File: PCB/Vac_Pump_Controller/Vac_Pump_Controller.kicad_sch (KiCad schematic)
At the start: 21 parts, among them J1 Conn_01x04_Socket, J1A Conn_01x04_Pin, J2 Conn_01x02_Socket, J2A Conn_01x02_Pin, J3 Conn_01x08_Socket, J3A Conn_01x08_Pin, J4 AC Plug, J5 DIN-6, J6 Conn_01x06_Socket, J6A Conn_01x06_Pin, J7 DIN-6, K1 Dual Relay Module, SW1 RotaryEncoder_Switch_MP, SW2 Pwr Switch, U1 WeMos D1 Mini32, U2 JXI 1.28in Round LCD

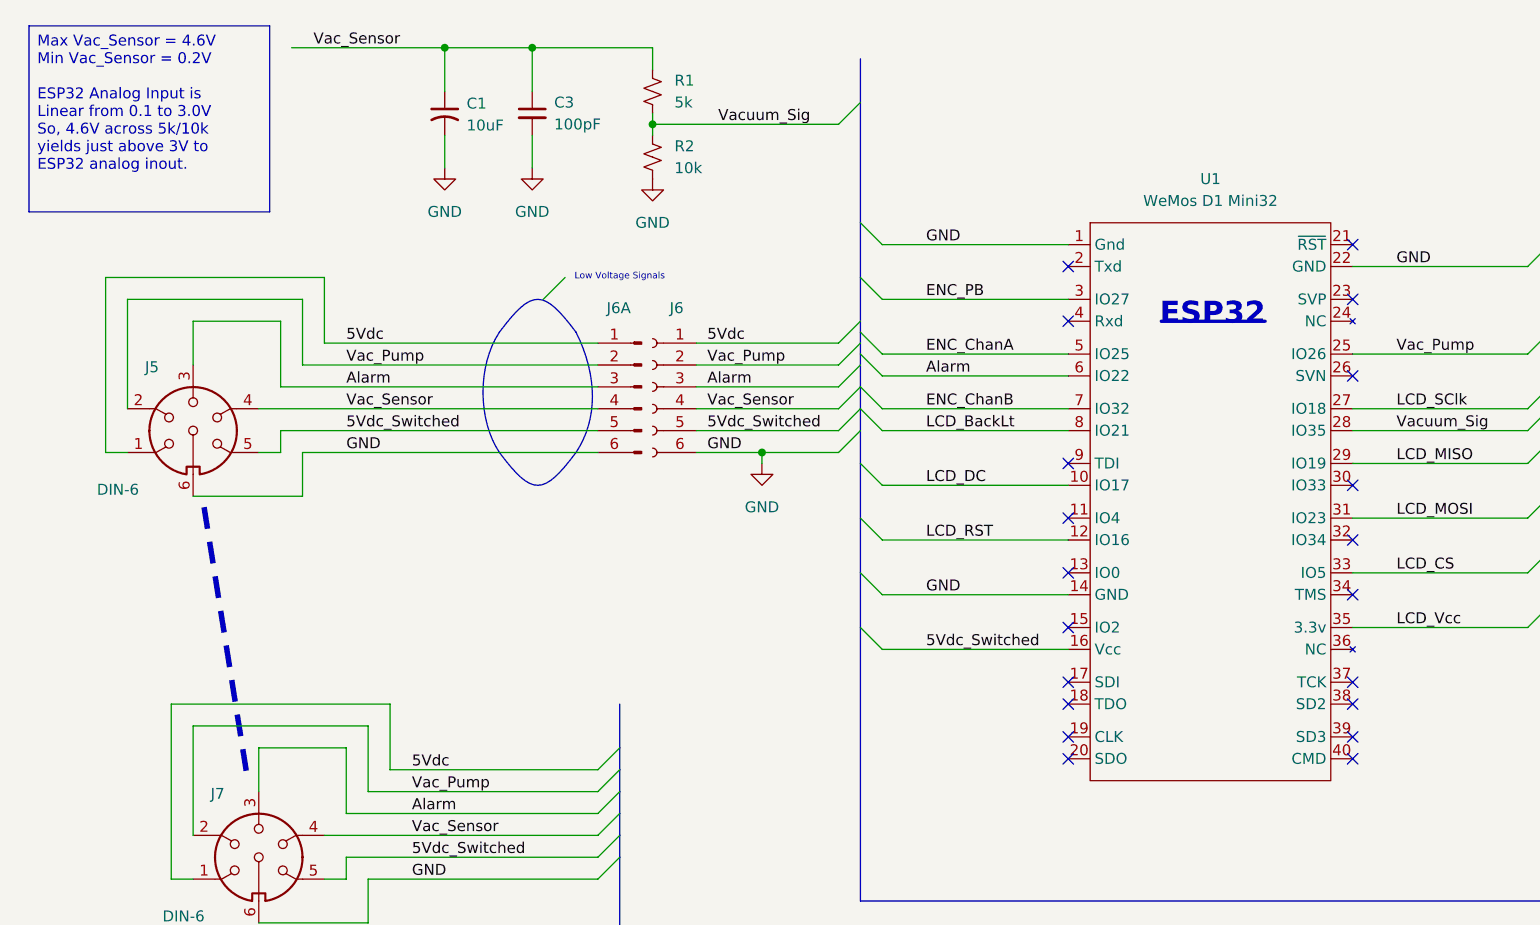
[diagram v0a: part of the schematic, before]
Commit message: PCB: swap ESP32 WeMos symbol for P-NUCLEO-WB55 (ST Morpho) in schematic
In-place symbol clone keeps identical pin geometry so every existing wire,
net-label and no-connect stays attached. Pin names -> WB55 functions, pin
numbers -> ST Morpho refs (CN7/CN10). Validated: kicad-cli sch erc reports
40 violations, identical to the pre-swap baseline (zero new). MCU power stays
on 5Vdc_Switched; MISO kept but marked n/c (write-only panel).

Co-Authored-By: Claude Opus 4.8 (1M context) <noreply@anthropic.com>
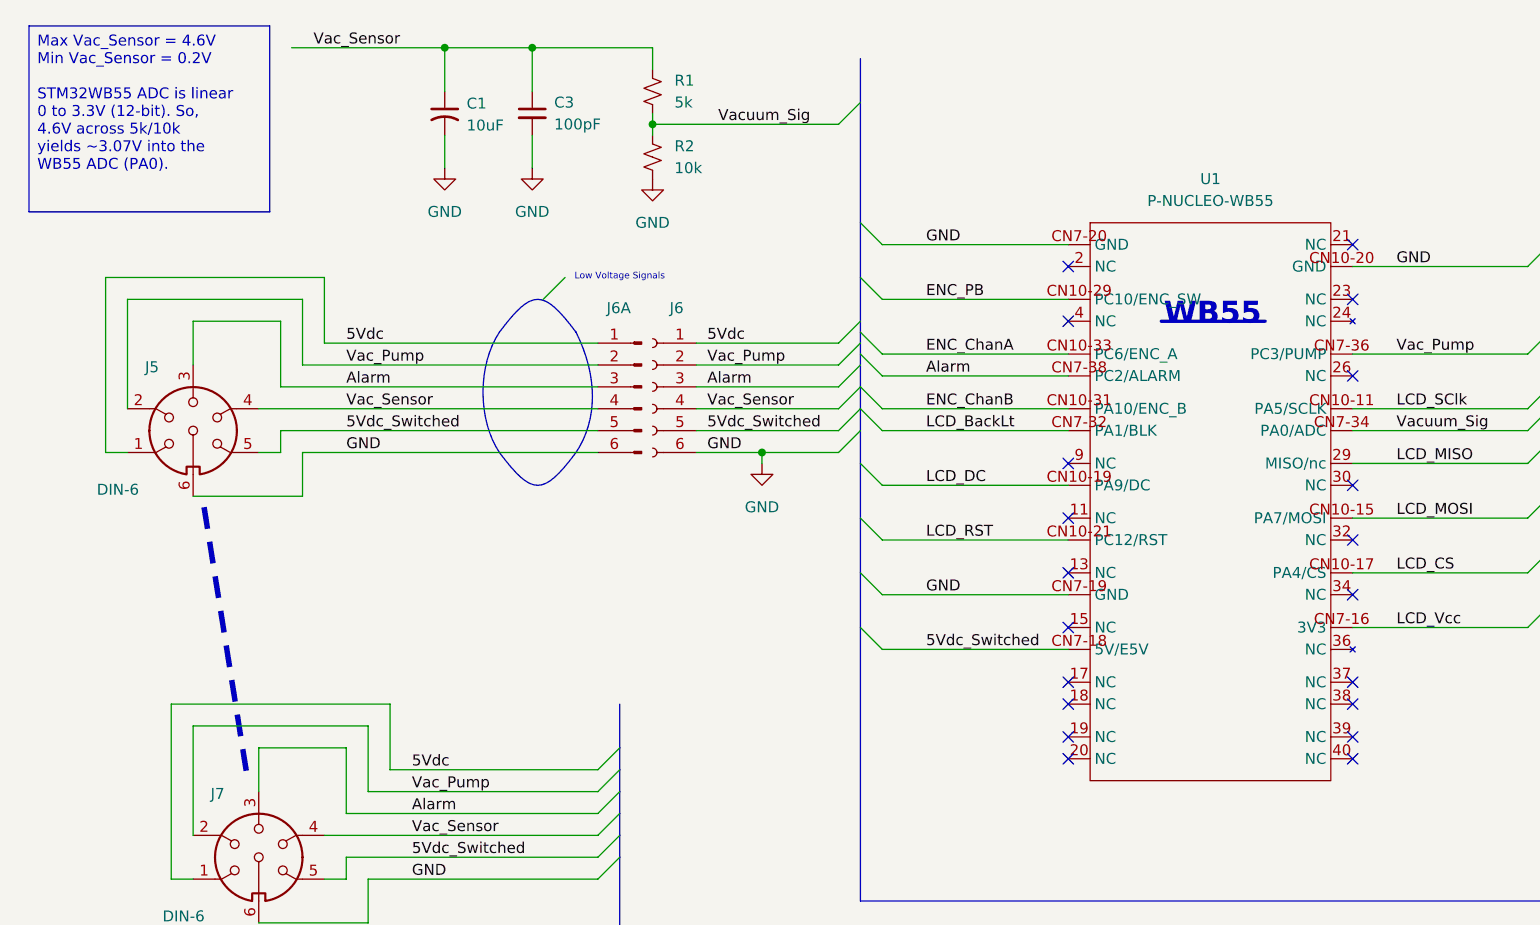
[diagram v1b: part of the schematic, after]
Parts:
- U1: value WeMos D1 Mini32 -> P-NUCLEO-WB55; symbol JK_And_Sons:WeMos_D1_Mini32 -> JK_And_Sons:P_NUCLEO_WB55
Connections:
- net 5Vdc_Switched: now also U1.CN7-18 (5V/E5V); no longer U1.16 (Vcc)
- net Alarm: now also U1.CN7-38 (PC2/ALARM); no longer U1.6 (IO22)
- net ENC_ChanA: now also U1.CN10-33 (PC6/ENC_A); no longer U1.5 (IO25)
- net ENC_ChanB: now also U1.CN10-31 (PA10/ENC_B); no longer U1.7 (IO32)
- net ENC_PB: now also U1.CN10-29 (PC10/ENC_SW); no longer U1.3 (IO27)
- net GND: now also U1.CN10-20 (GND), U1.CN7-19 (GND), U1.CN7-20 (GND); no longer U1.1 (Gnd), U1.14 (GND), U1.22 (GND)
- net LCD_BackLt: now also U1.CN7-32 (PA1/BLK); no longer U1.8 (IO21)
- net LCD_CS: now also U1.CN10-17 (PA4/CS); no longer U1.33 (IO5)
- net LCD_DC: now also U1.CN10-19 (PA9/DC); no longer U1.10 (IO17)
- net LCD_MOSI: now also U1.CN10-15 (PA7/MOSI); no longer U1.31 (IO23)
- net LCD_RST: now also U1.CN10-21 (PC12/RST); no longer U1.12 (IO16)
- net LCD_SClk: now also U1.CN10-11 (PA5/SCLK); no longer U1.27 (IO18)
- net LCD_Vcc: now also U1.CN7-16 (3V3); no longer U1.35 (3.3v)
- net Vac_Pump: now also U1.CN7-36 (PC3/PUMP); no longer U1.25 (IO26)
- net Vacuum_Sig: now also U1.CN7-34 (PA0/ADC); no longer U1.28 (IO35)
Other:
- note added: "WB55"
- note removed: "ESP32"
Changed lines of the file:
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@@
 		)
 	)
-	(text "ESP32"
+	(text "WB55"
 		(exclude_from_sim no)
 		(at 153.924 50.038 0)
@@
 		)
 	)
-	(text_box "Max Vac_Sensor = 4.6V\nMin Vac_Sensor = 0.2V\n\nESP32 Analog Input is\nLinear from 0.1 to 3.0V\nSo, 4.6V across 5k/10k\nyields just above 3V to\nESP32 analog inout."
+	(text_box "Max Vac_Sensor = 4.6V\nMin Vac_Sensor = 0.2V\n\nSTM32WB55 ADC is linear\n0 to 3.3V (12-bit). So,\n4.6V across 5k/10k\nyields ~3.07V into the\nWB55 ADC (PA0)."
 		(exclude_from_sim no)
 		(at 16.51 16.51 0)
@@
 	)
 	(symbol
-		(lib_id "JK_And_Sons:WeMos_D1_Mini32")
+		(lib_id "JK_And_Sons:P_NUCLEO_WB55")
 		(at 139.7 39.37 0)
 		(unit 1)
@@
 			)
 		)
-		(property "Value" "WeMos D1 Mini32"
+		(property "Value" "P-NUCLEO-WB55"
 			(at 153.67 36.83 0)
 			(effects
@@
 		(pin "21"
 		)
-		(pin "22"
+		(pin "CN10-20"
 		)
 		(pin "23"
@@
 		(pin "24"
 		)
-		(pin "25"
+		(pin "CN7-36"
 		)
 		(pin "26"
 		)
-		(pin "27"
+		(pin "CN10-11"
 		)
-		(pin "28"
+		(pin "CN7-34"
 		)
 		(pin "29"
@@
 		(pin "30"
 		)
-		(pin "31"
+		(pin "CN10-15"
 		)
 		(pin "32"
 		)
-		(pin "33"
+		(pin "CN10-17"
 		)
 		(pin "18"
@@
 		(pin "34"
 		)
-		(pin "35"
+		(pin "CN7-16"
 		)
 		(pin "19"
@@
 		(pin "20"
 		)
-		(pin "16"
+		(pin "CN7-18"
 		)
 		(pin "17"
@@
 		(pin "11"
 		)
-		(pin "3"
+		(pin "CN10-29"
 		)
-		(pin "14"
+		(pin "CN7-19"
 		)
 		(pin "2"
@@
 		(pin "13"
 		)
-		(pin "5"
+		(pin "CN10-33"
 		)
 		(pin "9"
 		)
-		(pin "12"
+		(pin "CN10-21"
 		)
-		(pin "6"
+		(pin "CN7-38"
 		)
-		(pin "1"
+		(pin "CN7-20"
 		)
 		(pin "36"
@@
 		(pin "4"
 		)
-		(pin "7"
+		(pin "CN10-31"
 		)
-		(pin "10"
+		(pin "CN10-19"
 		)
-		(pin "8"
+		(pin "CN7-32"
 		)
 		(instances

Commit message: PCB: tidy WB55 symbol label placement
Move the U1 net-labels outward along their existing wire stubs (right column
+12.7mm, left column -3.8mm) so they clear the longer WB55 pin numbers, and
remove the redundant 'WB55' watermark that overlapped two pin names. Only label
positions changed (wires/pins untouched) -> ERC unchanged at 40 (baseline) and
netlist connectivity verified identical (16 nets on U1, Morpho pin refs intact).

Co-Authored-By: Claude Opus 4.8 (1M context) <noreply@anthropic.com>
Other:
- note removed: "WB55"

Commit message: EVT1: calibrate vacuum readout + sensor front-end decoupling
Firmware (stm32/zephyrwb):
- Compile out CONFIG_VAC_SIM: read the real MPXV4115V on PA0/ADC1_IN5.
- Two-point calibration of the readout against the VB2200 manifold gauge with
  the fitted 3.94k/6.8k divider: atmosphere = 0 inHg @ 4044 counts, full vacuum
  = 29 inHg @ 709 counts (divider ratio and VREF cancel in the fit).
- Fix the gauge needle to track the calibrated value on the correct face angle
  (0 inHg at dial start, 30 under vacuum), aligned with the setpoint bugs.
- Enable CONFIG_LV_COLOR_16_SWAP to fix the GC9A01 RGB565 byte-swap color cast.

PCB (Vac_Pump_Controller):
- New Sensor_End hierarchical sheet: 3-pin MPXV4115V header with 10uF + 10nF
  supply decoupling and a 4-conductor cable connector back to the WB55.
- Add C4 10nF from the ADC divider tap to GND at the MCU (S&H / anti-alias).

.gitignore: exclude editor local-history and KiCad reports/lock files.

Co-Authored-By: Claude Opus 4.8 <noreply@anthropic.com>
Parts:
- added C4: 10nF, symbol Device:C_Small_US
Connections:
- net GND: now also C4.2
- net Vacuum_Sig: now also C4.1
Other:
- added sheet Sensor_End (Sensor_End.kicad_sch)
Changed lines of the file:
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@@
+		)
+	)
+	(wire
+		(pts
+			(xy 97.79 27.94) (xy 97.79 31.75)
+		)
+		(stroke
+			(width 0)
+			(type default)
+		)
+	)
+	(wire
+		(pts
+			(xy 97.79 36.83) (xy 97.79 39.37)
+		)
+		(stroke
+			(width 0)
+			(type default)
+		)
+	)
+	(junction
+		(at 97.79 27.94)
+		(diameter 0)
+		(color 0 0 0 0)
+	)
+	(symbol
+		(lib_id "Device:C_Small_US")
+		(at 97.79 34.29 0)
+		(unit 1)
+		(body_style 1)
+		(exclude_from_sim no)
+		(in_bom yes)
+		(on_board yes)
+		(in_pos_files yes)
+		(dnp no)
+		(fields_autoplaced yes)
+		(property "Reference" "C4"
+			(at 100.33 33.0238 0)
+			(show_name no)
+			(do_not_autoplace no)
+			(effects
+				(font
+					(size 1.27 1.27)
+				)
+				(justify left)
+			)
+		)
+		(property "Value" "10nF"
+			(at 100.33 35.5638 0)
+			(show_name no)
+			(do_not_autoplace no)
+			(effects
+				(font
+					(size 1.27 1.27)
+				)
+				(justify left)
+			)
+		)
+		(property "Footprint" ""
+			(at 97.79 34.29 0)
+			(hide yes)
+			(show_name no)
+			(do_not_autoplace no)
+			(effects
+				(font
+					(size 1.27 1.27)
+				)
+			)
+		)
+		(property "Datasheet" ""
+			(at 97.79 34.29 0)
+			(hide yes)
+			(show_name no)
+			(do_not_autoplace no)
+			(effects
+				(font
+					(size 1.27 1.27)
+				)
+			)
+		)
+		(property "Description" "Unpolarized capacitor, small symbol"
+			(at 97.79 34.29 0)
+			(hide yes)
+			(show_name no)
+			(do_not_autoplace no)
+			(effects
+				(font
+					(size 1.27 1.27)
+				)
+			)
+		)
+		(pin "1"
+		)
+		(pin "2"
+		)
+		(instances
+			(project "Vac_Pump_Controller"
+				(path "/72b54f5f-b695-431e-96f3-243cd740aa60"
+					(reference "C4")
+					(unit 1)
+				)
+			)
+		)
+	)
+	(symbol
+		(lib_id "power:GND")
+		(at 97.79 39.37 0)
+		(unit 1)
+		(body_style 1)
+		(exclude_from_sim no)
+		(in_bom yes)
+		(on_board yes)
+		(in_pos_files yes)
+		(dnp no)
+		(fields_autoplaced yes)
+		(property "Reference" "#PWR08"
+			(at 97.79 45.72 0)
+			(show_name no)
+			(do_not_autoplace no)
+			(hide yes)
+			(effects
+				(font
+					(size 1.27 1.27)
+				)
+			)
+		)
+		(property "Value" "GND"
+			(at 97.79 43.18 0)
+			(show_name no)
+			(do_not_autoplace no)
+			(effects
+				(font
+					(size 1.27 1.27)
+				)
+			)
+		)
+		(property "Footprint" ""
+			(at 97.79 39.37 0)
+			(show_name no)
+			(do_not_autoplace no)
+			(hide yes)
+			(effects
+				(font
+					(size 1.27 1.27)
+				)
+			)
+		)
+		(property "Datasheet" ""
+			(at 97.79 39.37 0)
+			(show_name no)
+			(do_not_autoplace no)
+			(hide yes)
+			(effects
+				(font
+					(size 1.27 1.27)
+				)
+			)
+		)
+		(pin "1"
+		)
+		(instances
+			(project "Vac_Pump_Controller"
+				(path "/72b54f5f-b695-431e-96f3-243cd740aa60"
+					(reference "#PWR08")
+					(unit 1)
+				)
+			)
+		)
+	)
+	(sheet
+		(at 152.4 152.4)
+		(size 33.02 20.32)
+		(exclude_from_sim no)
+		(in_bom yes)
+		(on_board yes)
+		(dnp no)
+		(fields_autoplaced yes)
+		(stroke
+			(width 0.1524)
+			(type solid)
+		)
+		(fill
+			(color 0 0 0 0.0000)
+		)
+		(property "Sheetname" "Sensor_End"
+			(at 152.4 151.6284 0)
+			(effects
+				(font
+					(size 1.27 1.27)
+				)
+				(justify left bottom)
+			)
+		)
+		(property "Sheetfile" "Sensor_End.kicad_sch"
+			(at 152.4 173.2416 0)
+			(effects
+				(font
+					(size 1.27 1.27)
+				)
+				(justify left top)
+			)
+		)
+		(instances
+			(project "Vac_Pump_Controller"
+				(path "/72b54f5f-b695-431e-96f3-243cd740aa60"
+					(page "2")
+				)
+			)
 		)
 	)
@@
 			(page "1")
 		)
-	)
+		(path "/a1b2c3d4-0002-4002-8002-000000000002"
+			(page "2")
+		)
+	)
